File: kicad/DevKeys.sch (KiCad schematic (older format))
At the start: 22 parts, among them SW1 SWITCH_PUSH, SW10 SWITCH_PUSH, SW2 SWITCH_PUSH, SW3 SWITCH_PUSH, SW4 SWITCH_PUSH, SW5 SWITCH_PUSH, SW6 SWITCH_PUSH, SW7 SWITCH_PUSH, SW8 SWITCH_PUSH, SW9 SWITCH_PUSH, U1 ARDUINO_MICRO_SHIELD

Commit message: dioden vor den Tasten entfernt
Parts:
- removed D1, D10, D2, D3, D4, D5, D6, D7, D8, D9: DIODE, footprints:DIODE, symbol DIODE
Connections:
- wire segments 55 -> 53
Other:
- moved on the sheet: SW1, SW2, SW3, SW4, SW5

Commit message: finished layout for first prototype pcb
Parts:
- SW1, SW10, SW2, SW3, SW4, SW5, SW6, SW7, SW8, SW9: footprint footprints:CHERRY_PCB_150H -> footprints:CHERRY_PCB_100H
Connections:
- net labels added: GND
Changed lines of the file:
@@
 F 0 "SW1" H 3950 4210 50  0000 C CNN
 F 1 "SWITCH_PUSH" H 3800 4020 50  0000 C CNN
-F 2 "footprints:CHERRY_PCB_150H" H 3800 4100 60  0001 C CNN
+F 2 "footprints:CHERRY_PCB_100H" H 3800 4100 60  0001 C CNN
 F 3 "" H 3800 4100 60  0000 C CNN
 	1    3800 4100
@@
 F 0 "SW2" H 3950 4610 50  0000 C CNN
 F 1 "SWITCH_PUSH" H 3800 4420 50  0000 C CNN
-F 2 "footprints:CHERRY_PCB_150H" H 3800 4500 60  0001 C CNN
+F 2 "footprints:CHERRY_PCB_100H" H 3800 4500 60  0001 C CNN
 F 3 "" H 3800 4500 60  0000 C CNN
 	1    3800 4500
@@
 F 0 "SW3" H 3950 4960 50  0000 C CNN
 F 1 "SWITCH_PUSH" H 3800 4770 50  0000 C CNN
-F 2 "footprints:CHERRY_PCB_150H" H 3800 4850 60  0001 C CNN
+F 2 "footprints:CHERRY_PCB_100H" H 3800 4850 60  0001 C CNN
 F 3 "" H 3800 4850 60  0000 C CNN
 	1    3800 4850
@@
 F 0 "SW4" H 3950 5310 50  0000 C CNN
 F 1 "SWITCH_PUSH" H 3800 5120 50  0000 C CNN
-F 2 "footprints:CHERRY_PCB_150H" H 3800 5200 60  0001 C CNN
+F 2 "footprints:CHERRY_PCB_100H" H 3800 5200 60  0001 C CNN
 F 3 "" H 3800 5200 60  0000 C CNN
 	1    3800 5200
@@
 F 0 "SW5" H 3950 5710 50  0000 C CNN
 F 1 "SWITCH_PUSH" H 3800 5520 50  0000 C CNN
-F 2 "footprints:CHERRY_PCB_150H" H 3800 5600 60  0001 C CNN
+F 2 "footprints:CHERRY_PCB_100H" H 3800 5600 60  0001 C CNN
 F 3 "" H 3800 5600 60  0000 C CNN
 	1    3800 5600
@@
 F 0 "SW6" H 4900 4210 50  0000 C CNN
 F 1 "SWITCH_PUSH" H 4750 4020 50  0000 C CNN
-F 2 "footprints:CHERRY_PCB_150H" H 4750 4100 60  0001 C CNN
+F 2 "footprints:CHERRY_PCB_100H" H 4750 4100 60  0001 C CNN
 F 3 "" H 4750 4100 60  0000 C CNN
 	1    4750 4100
@@
 F 0 "SW7" H 4900 4560 50  0000 C CNN
 F 1 "SWITCH_PUSH" H 4750 4370 50  0000 C CNN
-F 2 "footprints:CHERRY_PCB_150H" H 4750 4450 60  0001 C CNN
+F 2 "footprints:CHERRY_PCB_100H" H 4750 4450 60  0001 C CNN
 F 3 "" H 4750 4450 60  0000 C CNN
 	1    4750 4450
@@
 F 0 "SW8" H 4900 4910 50  0000 C CNN
 F 1 "SWITCH_PUSH" H 4750 4720 50  0000 C CNN
-F 2 "footprints:CHERRY_PCB_150H" H 4750 4800 60  0001 C CNN
+F 2 "footprints:CHERRY_PCB_100H" H 4750 4800 60  0001 C CNN
 F 3 "" H 4750 4800 60  0000 C CNN
 	1    4750 4800
@@
 F 0 "SW9" H 4900 5310 50  0000 C CNN
 F 1 "SWITCH_PUSH" H 4750 5120 50  0000 C CNN
-F 2 "footprints:CHERRY_PCB_150H" H 4750 5200 60  0001 C CNN
+F 2 "footprints:CHERRY_PCB_100H" H 4750 5200 60  0001 C CNN
 F 3 "" H 4750 5200 60  0000 C CNN
 	1    4750 5200
@@
 F 0 "SW10" H 4900 5710 50  0000 C CNN
 F 1 "SWITCH_PUSH" H 4750 5520 50  0000 C CNN
-F 2 "footprints:CHERRY_PCB_150H" H 4750 5600 60  0001 C CNN
+F 2 "footprints:CHERRY_PCB_100H" H 4750 5600 60  0001 C CNN
 F 3 "" H 4750 5600 60  0000 C CNN
 	1    4750 5600
@@
 	4450 4100 4450 3700
 Connection ~ 4450 3700
+Text Label 6900 3700 0    60   ~ 0
+GND
 $EndSCHEMATC

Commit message: updated to new lib
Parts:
- RV1: symbol POT -> POT-RESCUE-DevKeys
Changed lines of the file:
@@
 EESchema Schematic File Version 2
+LIBS:DevKeys-rescue
 LIBS:power
 LIBS:device
@@
 	6900 4400 7400 4400
 $Comp
-L POT RV1
+L POT-RESCUE-DevKeys RV1
 U 1 1 57B2949F
 P 9700 4250

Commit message: neues Platinen-Layout
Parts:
- removed RV1: POT, Potentiometers:Potentiometer_WirePads, symbol POT-RESCUE-DevKeys
- removed SW1, SW10, SW2, SW3, SW4, SW5, SW6, SW7, SW8, SW9: SWITCH_PUSH, footprints:CHERRY_PCB_100H, symbol SWITCH_PUSH
- removed U1: ARDUINO_MICRO_SHIELD, arduino_micro_shield:ARDUINO_MICRO_SHIELD, symbol ARDUINO_MICRO_SHIELD
- added J1: RaspberryPiZeroW, Pin_Headers:Pin_Header_Straight_2x20_Pitch2.54mm, symbol Conn_02x20_Odd_Even
- added J2: Display, Socket_Strips:Socket_Strip_Straight_1x04_Pitch2.54mm, symbol Conn_01x04_Female
- added S1: KeyStart, mx1a:MX1A, symbol MX1A
- added S10: KeyEvaluateSelection, mx1a:MX1A, symbol MX1A
- added S2: KeyStop, mx1a:MX1A, symbol MX1A
- added S3: KeySelect, mx1a:MX1A, symbol MX1A
- added S4: KeyStepOver, mx1a:MX1A, symbol MX1A
- added S5: KeyStepInto, mx1a:MX1A, symbol MX1A
- added S6: KeyStepOut, mx1a:MX1A, symbol MX1A
- added S7: KeyRunToCursor, mx1a:MX1A, symbol MX1A
- added S8: KeyRunSection, mx1a:MX1A, symbol MX1A
- added S9: KeyRunAndAdvance, mx1a:MX1A, symbol MX1A
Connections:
- new net: J1.10 (Pin_10), S2.2
- new net: J1.12 (Pin_12), S3.2
- new net: J1.17 (Pin_17), J2.3 (Pin_3)
- new net: J1.20 (Pin_20), J2.4 (Pin_4), S4.1, S5.1, S6.1
- new net: J1.22 (Pin_22), S4.2
- new net: J1.24 (Pin_24), S5.2
- new net: J1.26 (Pin_26), S6.2
- new net: J1.3 (Pin_3), J2.1 (Pin_1)
- new net: J1.30 (Pin_30), S10.1, S7.1, S8.1, S9.1
- new net: J1.32 (Pin_32), S7.2
- new net: J1.36 (Pin_36), S8.2
- new net: J1.38 (Pin_38), S9.2
- new net: J1.40 (Pin_40), S10.2
- new net: J1.5 (Pin_5), J2.2 (Pin_2)
- new net: J1.6 (Pin_6), S1.1, S2.1, S3.1
- new net: J1.8 (Pin_8), S1.2

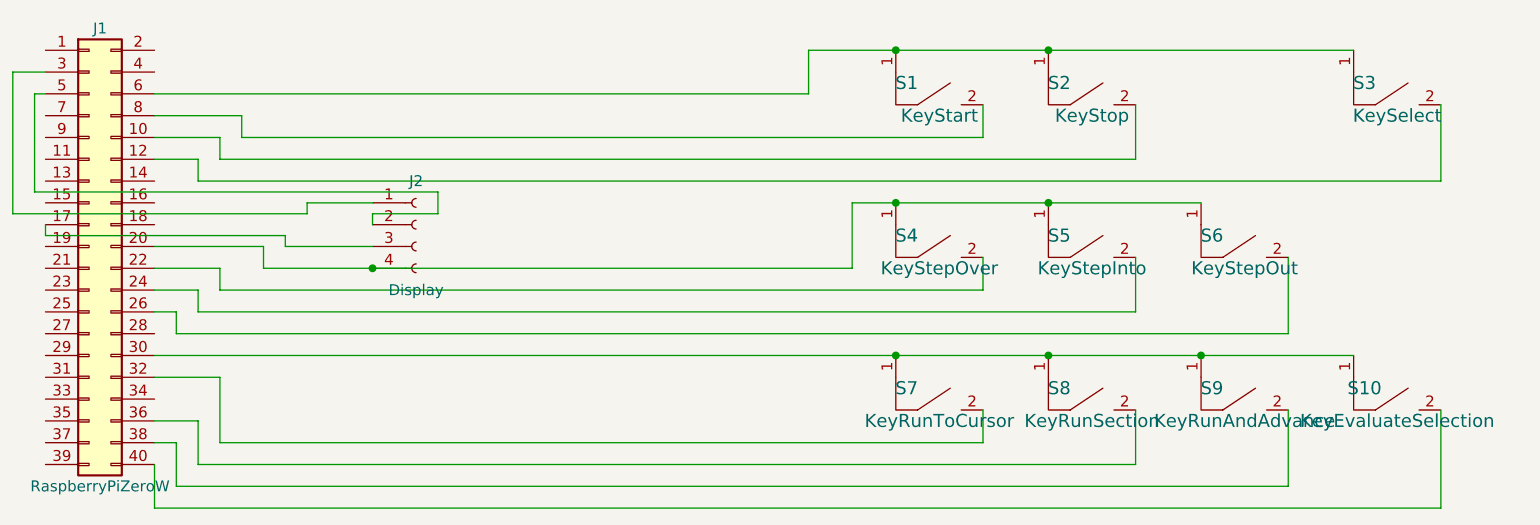
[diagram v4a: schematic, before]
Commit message: Layout angepasst zum ätzen.
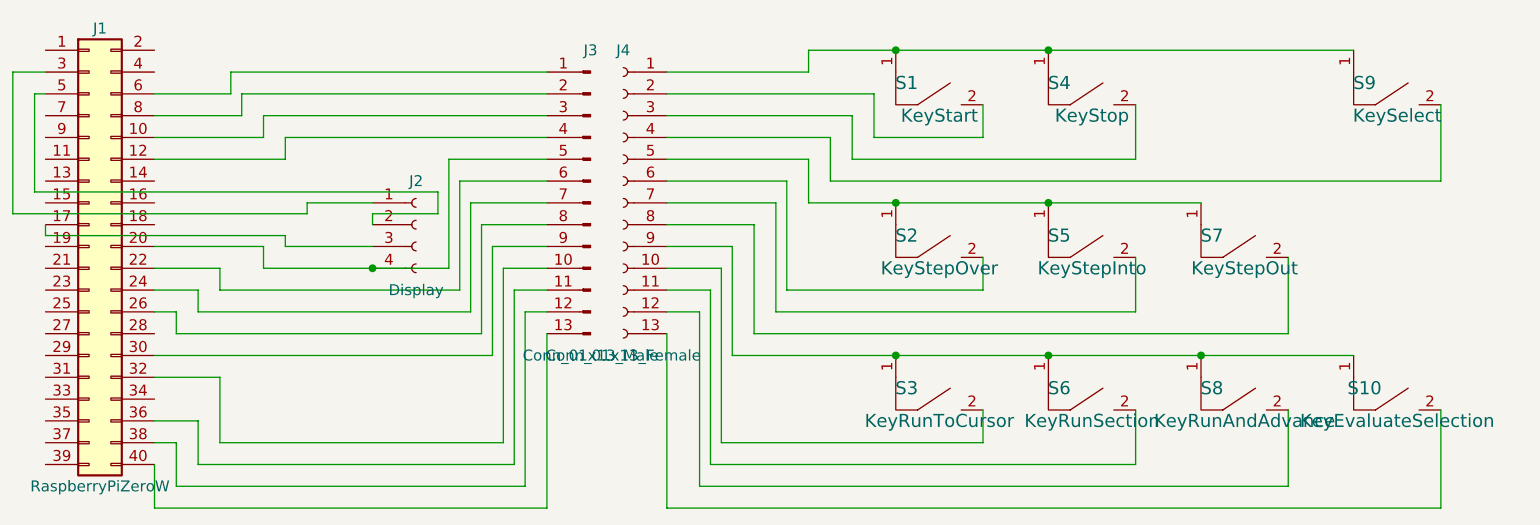
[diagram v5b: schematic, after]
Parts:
- added J3: Conn_01x13_Male, Pin_Headers:Pin_Header_Angled_1x13_Pitch2.54mm, symbol Conn_01x13_Male
- added J4: Conn_01x13_Female, Pin_Headers:Pin_Header_Straight_1x13_Pitch2.54mm, symbol Conn_01x13_Female
- renumbered S4 to S2, S7 to S3, S2 to S4, S8 to S6, S6 to S7, S9 to S8, S3 to S9
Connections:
- net at J1.10 (Pin_10): now also J3.3 (Pin_3); no longer S4.2
- net at J1.12 (Pin_12): now also J3.4 (Pin_4); no longer S9.2
- net at S2.1, S5.1, S7.1: now also J4.5 (Pin_5); no longer J1.20 (Pin_20), J2.4 (Pin_4)
- net at J1.22 (Pin_22): now also J3.6 (Pin_6); no longer S2.2
- net at J1.24 (Pin_24): now also J3.7 (Pin_7); no longer S5.2
- net at J1.26 (Pin_26): now also J3.8 (Pin_8); no longer S7.2
- net at S10.1, S3.1, S6.1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: now also J4.9 (Pin_9); no longer J1.30 (Pin_30)
- net at J1.32 (Pin_32): now also J3.10 (Pin_10); no longer S3.2
- net at J1.36 (Pin_36): now also J3.11 (Pin_11); no longer S6.2
- net at J1.38 (Pin_38): now also J3.12 (Pin_12); no longer S8.2
- net at J1.40 (Pin_40): now also J3.13 (Pin_13); no longer S10.2
- net at S1.1, S4.1, S9.1: now also J4.1 (Pin_1); no longer J1.6 (Pin_6)
- net at J1.8 (Pin_8): now also J3.2 (Pin_2); no longer S1.2
- new net: J1.20 (Pin_20), J2.4 (Pin_4), J3.5 (Pin_5)
- new net: J1.30 (Pin_30), J3.9 (Pin_9)
- new net: J1.6 (Pin_6), J3.1 (Pin_1)
- new net: J4.6 (Pin_6), S2.2
- new net: J4.7 (Pin_7), S5.2
- new net: J4.2 (Pin_2), S1.2
- new net: J4.3 (Pin_3), S4.2
- new net: J4.8 (Pin_8), S7.2
- new net: J4.4 (Pin_4), S9.2
- new net: J4.10 (Pin_10), S3.2
- new net: J4.11 (Pin_11), S6.2
- new net: J4.12 (Pin_12), S8.2
- new net: J4.13 (Pin_13), S10.2
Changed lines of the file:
@@
 LIBS:mx1a
 LIBS:components
+LIBS:DevKeys-cache
 EELAYER 25 0
 EELAYER END
@@
 $EndComp
 $Comp
-L MX1A S4
+L MX1A S2
 U 1 1 5A969B31
 P 5400 2900
-F 0 "S4" H 5250 3150 60  0000 C CNN
+F 0 "S2" H 5250 3150 60  0000 C CNN
 F 1 "KeyStepOver" H 5400 3000 60  0000 C CNN
 F 2 "mx1a:MX1A" H 5400 2900 60  0001 C CNN
@@
 $EndComp
 $Comp
-L MX1A S2
+L MX1A S4
 U 1 1 5A96A02A
 P 6100 2200
-F 0 "S2" H 5950 2450 60  0000 C CNN
+F 0 "S4" H 5950 2450 60  0000 C CNN
 F 1 "KeyStop" H 6100 2300 60  0000 C CNN
 F 2 "mx1a:MX1A" H 6100 2200 60  0001 C CNN
@@
 $EndComp
 $Comp
-L MX1A S6
+L MX1A S7
 U 1 1 5A96A1F0
 P 6800 2900
-F 0 "S6" H 6650 3150 60  0000 C CNN
+F 0 "S7" H 6650 3150 60  0000 C CNN
 F 1 "KeyStepOut" H 6800 3000 60  0000 C CNN
 F 2 "mx1a:MX1A" H 6800 2900 60  0001 C CNN
@@
 $EndComp
 $Comp
-L MX1A S3
+L MX1A S9
 U 1 1 5A96A359
 P 7500 2200
-F 0 "S3" H 7350 2450 60  0000 C CNN
+F 0 "S9" H 7350 2450 60  0000 C CNN
 F 1 "KeySelect" H 7500 2300 60  0000 C CNN
 F 2 "mx1a:MX1A" H 7500 2200 60  0001 C CNN
@@
 $EndComp
 $Comp
-L MX1A S7
+L MX1A S3
 U 1 1 5A96A555
 P 5400 3600
-F 0 "S7" H 5250 3850 60  0000 C CNN
+F 0 "S3" H 5250 3850 60  0000 C CNN
 F 1 "KeyRunToCursor" H 5400 3700 60  0000 C CNN
 F 2 "mx1a:MX1A" H 5400 3600 60  0001 C CNN
@@
 $EndComp
 $Comp
-L MX1A S8
+L MX1A S6
 U 1 1 5A96A55B
 P 6100 3600
-F 0 "S8" H 5950 3850 60  0000 C CNN
+F 0 "S6" H 5950 3850 60  0000 C CNN
 F 1 "KeyRunSection" H 6100 3700 60  0000 C CNN
 F 2 "mx1a:MX1A" H 6100 3600 60  0001 C CNN
@@
 $EndComp
 $Comp
-L MX1A S9
+L MX1A S8
 U 1 1 5A96A561
 P 6800 3600
-F 0 "S9" H 6650 3850 60  0000 C CNN
+F 0 "S8" H 6650 3850 60  0000 C CNN
 F 1 "KeyRunAndAdvance" H 6800 3700 60  0000 C CNN
 F 2 "mx1a:MX1A" H 6800 3600 60  0001 C CNN
@@
 	2300 2700 2300 2800
 Wire Wire Line
-	2300 2800 5000 2800
-Wire Wire Line
 	2400 2700 2800 2700
 Wire Wire Line
@@
 	7000 3450 7000 3800
 Wire Wire Line
-	7700 3900 1800 3900
-Wire Wire Line
 	1800 3900 1800 3700
 Wire Wire Line
-	7000 3800 1900 3800
-Wire Wire Line
 	1900 3800 1900 3600
 Wire Wire Line
 	1900 3600 1800 3600
 Wire Wire Line
-	6300 3700 2000 3700
-Wire Wire Line
 	2000 3700 2000 3500
 Wire Wire Line
 	2000 3500 1800 3500
 Wire Wire Line
-	5600 3600 2100 3600
-Wire Wire Line
 	2100 3600 2100 3300
 Wire Wire Line
 	2100 3300 1800 3300
-Wire Wire Line
-	1800 3200 7300 3200
 Connection ~ 5200 3200
 Connection ~ 5900 3200
@@
 	5600 2750 5600 2900
 Wire Wire Line
-	7000 3100 1900 3100
-Wire Wire Line
 	1900 3100 1900 3000
 Wire Wire Line
 	1900 3000 1800 3000
 Wire Wire Line
-	6300 3000 2000 3000
-Wire Wire Line
 	2000 3000 2000 2900
 Wire Wire Line
 	2000 2900 1800 2900
 Wire Wire Line
-	5600 2900 2100 2900
-Wire Wire Line
 	2100 2900 2100 2800
 Wire Wire Line
 	2100 2800 1800 2800
 Wire Wire Line
-	5000 2800 5000 2500
-Wire Wire Line
-	5000 2500 6600 2500
+	4800 2500 6600 2500
 Connection ~ 2800 2800
 Connection ~ 5200 2500
@@
 	7700 2050 7700 2400
 Wire Wire Line
-	7700 2400 2000 2400
-Wire Wire Line
-	2000 2400 2000 2300
-Wire Wire Line
-	2000 2300 1800 2300
-Wire Wire Line
-	1800 2200 2100 2200
-Wire Wire Line
-	2100 2200 2100 2300
-Wire Wire Line
-	2100 2300 6300 2300
-Wire Wire Line
-	5600 2200 2200 2200
-Wire Wire Line
-	2200 2200 2200 2100
-Wire Wire Line
-	2200 2100 1800 2100
-Wire Wire Line
-	1800 2000 4800 2000
-Wire Wire Line
-	4800 2000 4800 1800
-Wire Wire Line
 	4800 1800 7300 1800
 Connection ~ 5200 1800
@@
 Wire Wire Line
 	1250 2000 1300 2000
+$Comp
+L Conn_01x13_Male J3
+U 1 1 5AB62A89
+P 3800 2500
+F 0 "J3" H 3800 3200 50  0000 C CNN
+F 1 "Conn_01x13_Male" H 3800 1800 50  0000 C CNN
+F 2 "Pin_Headers:Pin_Header_Angled_1x13_Pitch2.54mm" H 3800 2500 50  0001 C CNN
+F 3 "" H 3800 2500 50  0001 C CNN
+	1    3800 2500
+	-1   0    0    -1
+$EndComp
+$Comp
+L Conn_01x13_Female J4
+U 1 1 5AB62BCF
+P 3950 2500
+F 0 "J4" H 3950 3200 50  0000 C CNN
+F 1 "Conn_01x13_Female" H 3950 1800 50  0000 C CNN
+F 2 "Pin_Headers:Pin_Header_Straight_1x13_Pitch2.54mm" H 3950 2500 50  0001 C CNN
+F 3 "" H 3950 2500 50  0001 C CNN
+	1    3950 2500
+	-1   0    0    -1
+$EndComp
+Wire Wire Line
+	3600 1900 2150 1900
+Wire Wire Line
+	2150 1900 2150 2000
+Wire Wire Line
+	2150 2000 1800 2000
+Wire Wire Line
+	4150 1900 4800 1900
+Wire Wire Line
+	4800 1900 4800 1800
+Wire Wire Line
+	2200 2000 3600 2000
+Wire Wire Line
+	4150 2000 5100 2000
+Wire Wire Line
+	5100 2000 5100 2200
+Wire Wire Line
+	5100 2200 5600 2200
+Wire Wire Line
+	2300 2100 3600 2100
+Wire Wire Line
+	4150 2100 5000 2100
+Wire Wire Line
+	5000 2100 5000 2300
+Wire Wire Line
+	5000 2300 6300 2300
+Wire Wire Line
+	2400 2200 3600 2200
+Wire Wire Line
+	4150 2200 4900 2200
+Wire Wire Line
+	4900 2200 4900 2400
+Wire Wire Line
+	4900 2400 7700 2400
+Wire Wire Line
+	4800 2300 4800 2500
+Wire Wire Line
+	4150 2300 4800 2300
+Wire Wire Line
+	3150 2300 3600 2300
+Wire Wire Line
+	5600 2900 4700 2900
+Wire Wire Line
+	4700 2900 4700 2400
+Wire Wire Line
+	4700 2400 4150 2400
+Wire Wire Line
+	3200 2400 3600 2400
+Wire Wire Line
+	2200 2000 2200 2100
+Wire Wire Line
+	2200 2100 1800 2100
+Wire Wire Line
+	2300 2100 2300 2200
+Wire Wire Line
+	2300 2200 1800 2200
+Wire Wire Line
+	2400 2200 2400 2300
+Wire Wire Line
+	2400 2300 1800 2300
+Wire Wire Line
+	3150 2800 3150 2300
+Wire Wire Line
+	2300 2800 3150 2800
+Wire Wire Line
+	3200 2400 3200 2900
+Wire Wire Line
+	3200 2900 2100 2900
+Wire Wire Line
+	6300 3000 4650 3000
+Wire Wire Line
+	4650 3000 4650 2500
+Wire Wire Line
+	4650 2500 4150 2500
+Wire Wire Line
+	3600 2500 3250 2500
+Wire Wire Line
+	3250 2500 3250 3000
+Wire Wire Line
+	3250 3000 2000 3000
+Wire Wire Line
+	7000 3100 4550 3100
+Wire Wire Line
+	4550 3100 4550 2600
+Wire Wire Line
+	4550 2600 4150 2600
+Wire Wire Line
+	3600 2600 3300 2600
+Wire Wire Line
+	3300 2600 3300 3100
+Wire Wire Line
+	3300 3100 1900 3100
+Wire Wire Line
+	4450 3200 7300 3200
+Wire Wire Line
+	4450 3200 4450 2700
+Wire Wire Line
+	4450 2700 4150 2700
+Wire Wire Line
+	3350 2700 3600 2700
+Wire Wire Line
+	3350 2700 3350 3200
+Wire Wire Line
+	3350 3200 1800 3200
+Wire Wire Line
+	5600 3600 4400 3600
+Wire Wire Line
+	4400 3600 4400 2800
+Wire Wire Line
+	4400 2800 4150 2800
+Wire Wire Line
+	3600 2800 3400 2800
+Wire Wire Line
+	3400 2800 3400 3600
+Wire Wire Line
+	3400 3600 2100 3600
+Wire Wire Line
+	6300 3700 4350 3700
+Wire Wire Line
+	4350 3700 4350 2900
+Wire Wire Line
+	4350 2900 4150 2900
+Wire Wire Line
+	3600 2900 3450 2900
+Wire Wire Line
+	3450 2900 3450 3700
+Wire Wire Line
+	3450 3700 2000 3700
+Wire Wire Line
+	7000 3800 4300 3800
+Wire Wire Line
+	4300 3800 4300 3000
+Wire Wire Line
+	4300 3000 4150 3000
+Wire Wire Line
+	3600 3000 3500 3000
+Wire Wire Line
+	3500 3000 3500 3800
+Wire Wire Line
+	3500 3800 1900 3800
+Wire Wire Line
+	3600 3100 3600 3900
+Wire Wire Line
+	3600 3900 1800 3900
+Wire Wire Line
+	7700 3900 4150 3900
+Wire Wire Line
+	4150 3900 4150 3100
 $EndSCHEMATC
